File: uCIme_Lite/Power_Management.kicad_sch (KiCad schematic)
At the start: 17 parts

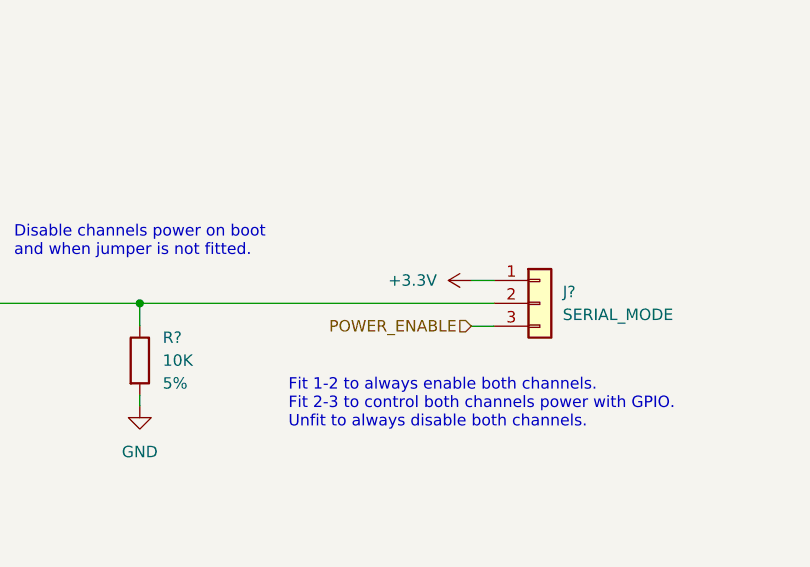
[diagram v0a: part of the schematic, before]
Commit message: lite: Used the +5V power supply for the power switch always-on mode instead of the +3.3V to ease routing.
Signed-off-by: Adrien Ricciardi <aricciardi@baylibre.com>
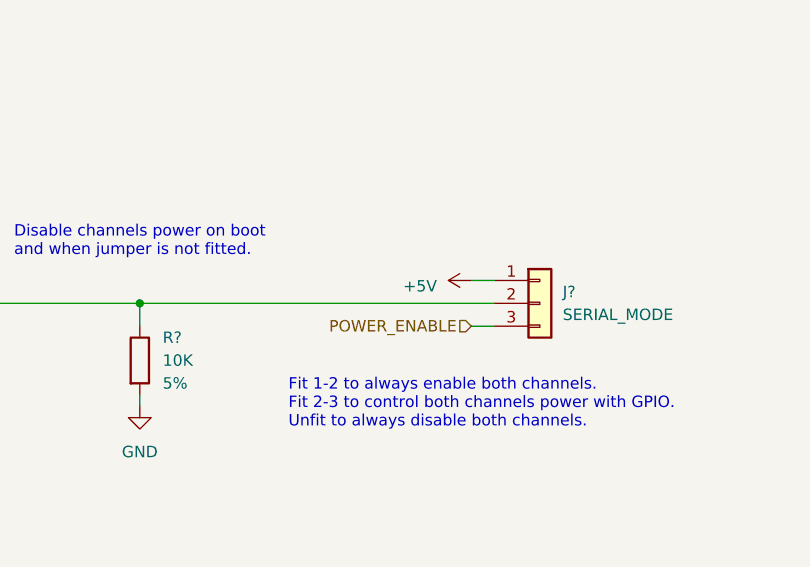
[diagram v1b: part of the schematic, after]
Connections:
- net +3.3V is gone; now on net +5V: J?.1 (Pin_1)
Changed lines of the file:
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@@
-    )
-  )
-  (symbol (lib_id "power:+3.3V") (at 250.19 58.42 90) (unit 1)
-    (in_bom yes) (on_board yes) (dnp no) (fields_autoplaced)
-    (property "Reference" "#PWR0117" (at 254 58.42 0)
-      (effects (font (size 1.27 1.27)) hide)
-    )
-    (property "Value" "+3.3V" (at 246.38 58.4199 90)
-      (effects (font (size 1.27 1.27)) (justify left))
-    )
-    (property "Footprint" "" (at 250.19 58.42 0)
-      (effects (font (size 1.27 1.27)) hide)
-    )
-    (property "Datasheet" "" (at 250.19 58.42 0)
-      (effects (font (size 1.27 1.27)) hide)
-    )
-    (pin "1")
-    (instances
-      (project "uCIme_Lite"
-        (path "/6d46d15a-8cd0-4983-b142-8248cafa0b56/b72074d7-db6e-4ce2-896d-216adccf1d19"
-          (reference "#PWR0117") (unit 1)
-        )
-      )
     )
   )
@@
         )
       )
+    )
+  )
+  (symbol (lib_id "power:+5V") (at 250.19 58.42 90) (unit 1)
+    (in_bom yes) (on_board yes) (dnp no) (fields_autoplaced)
+    (property "Reference" "#PWR01" (at 254 58.42 0)
+      (effects (font (size 1.27 1.27)) hide)
+    )
+    (property "Value" "+5V" (at 246.38 59.055 90)
+      (effects (font (size 1.27 1.27)) (justify left))
+    )
+    (property "Footprint" "" (at 250.19 58.42 0)
+      (effects (font (size 1.27 1.27)) hide)
+    )
+    (property "Datasheet" "" (at 250.19 58.42 0)
+      (effects (font (size 1.27 1.27)) hide)
+    )
+    (pin "1")
+    (instances
+      (project "uCIme_Lite"
+        (path "/6d46d15a-8cd0-4983-b142-8248cafa0b56/b72074d7-db6e-4ce2-896d-216adccf1d19"
+          (reference "#PWR01") (unit 1)
+        )
+      )

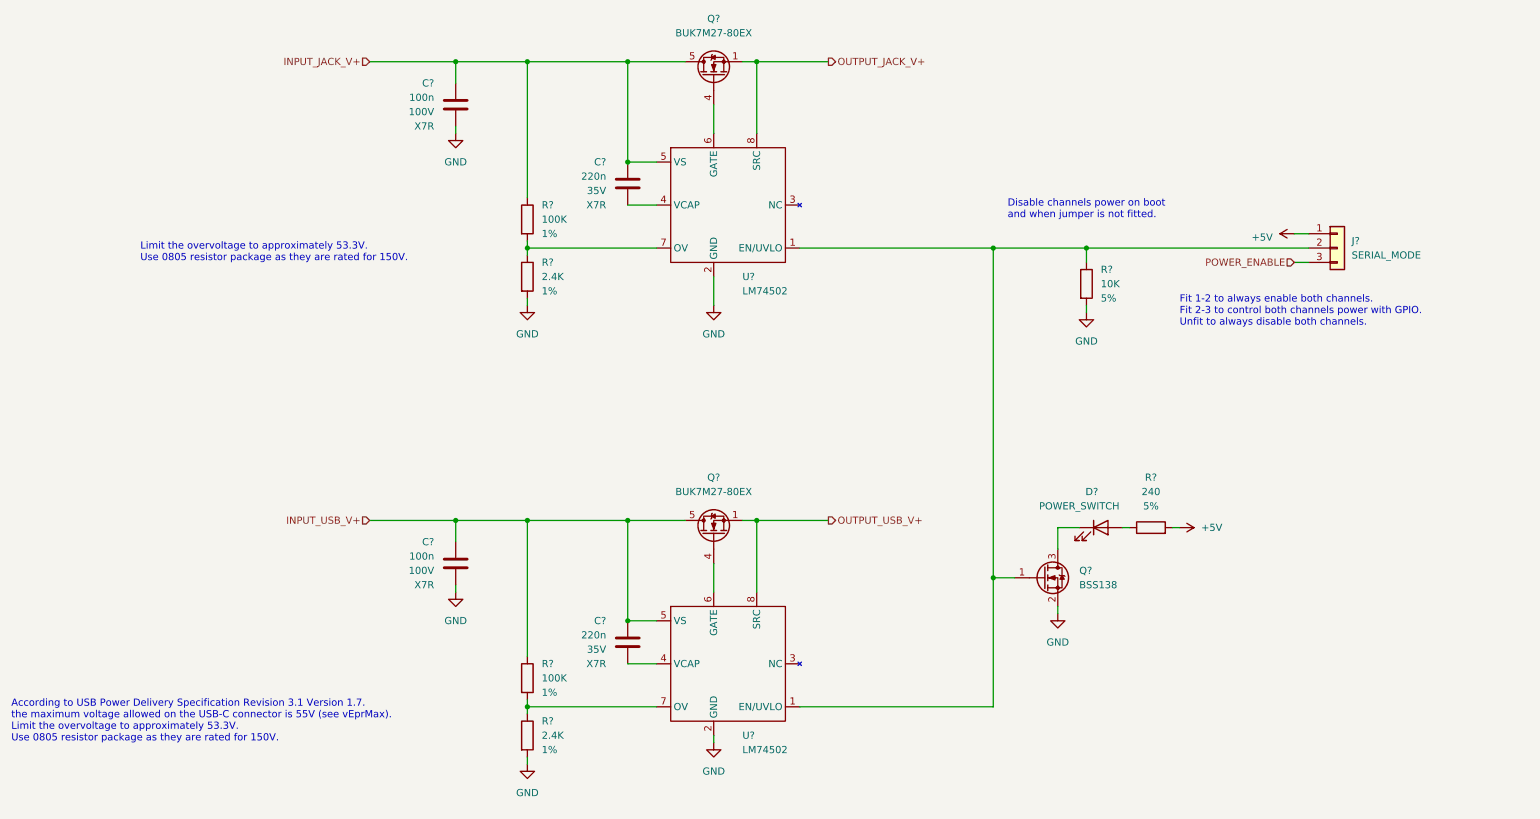
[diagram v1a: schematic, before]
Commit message: lite: Added a dedicated mode selection jumper per power channel. This allows to fit custom requirements, like disabling the USB power while keeping the USB connected and driving the board power with the jack channel.
Signed-off-by: Adrien Ricciardi <aricciardi@baylibre.com>
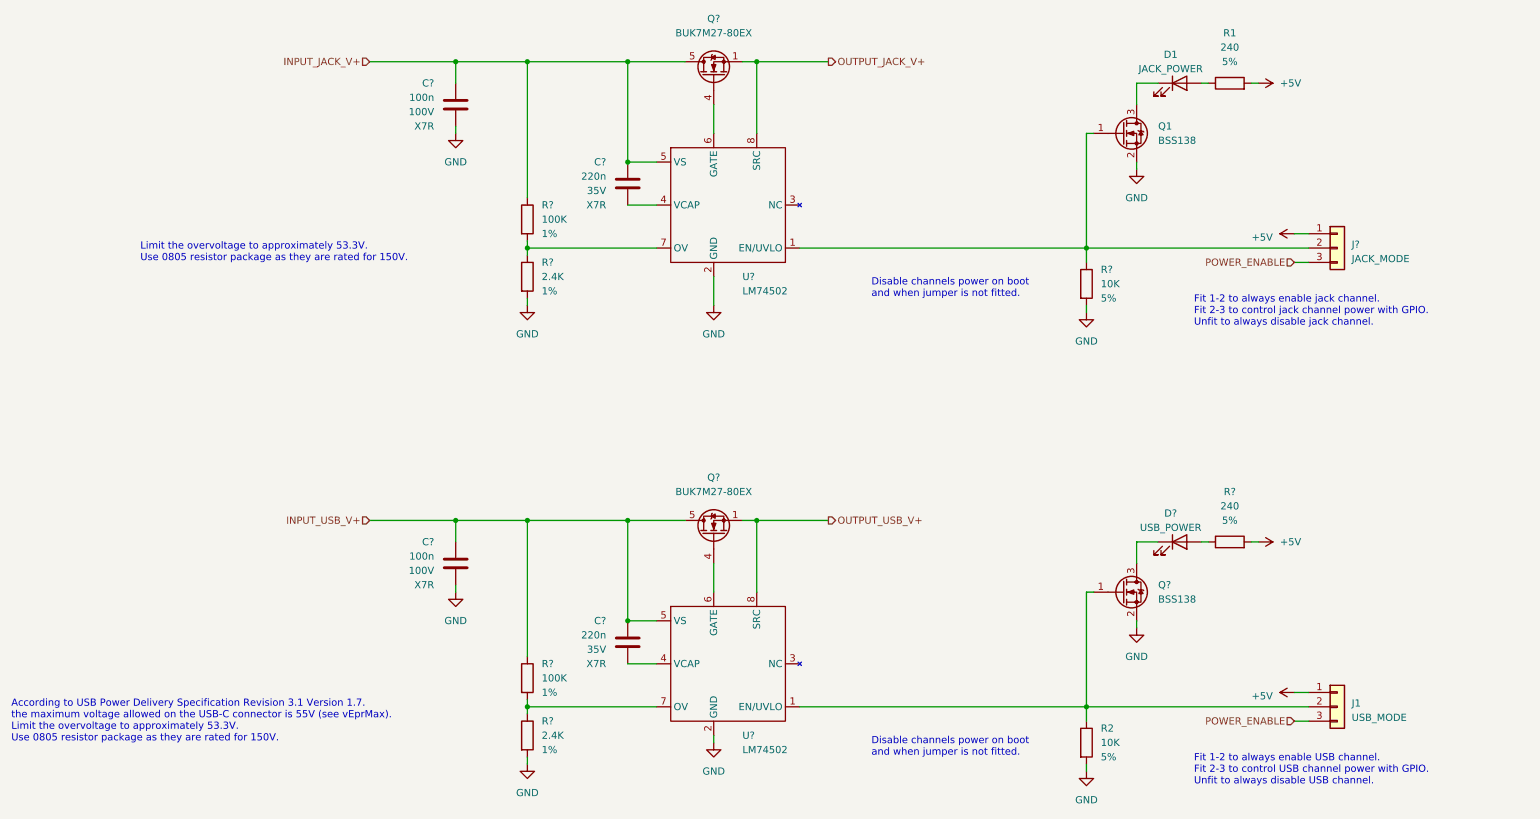
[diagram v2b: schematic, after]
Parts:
- added D1: POWER_SWITCH, symbol Device:LED
- added J1: USB_MODE, symbol Connector_Generic:Conn_01x03
- added Q1: BSS138, Package_TO_SOT_SMD:SOT-23, symbol Transistor_FET:BSS138
- added R1: 240, Resistor_SMD:R_1206_3216Metric, symbol Device:R
- added R2: 10K, Resistor_SMD:R_0603_1608Metric, symbol Device:R
- J?: value SERIAL_MODE -> JACK_MODE
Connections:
- net +5V: now also J1.1 (Pin_1), R1.2
- net GND: now also Q1.2 (S), R2.2
- net POWER_ENABLE: now also J1.3 (Pin_3)
- net at J?.2 (Pin_2), R?.1, U?.1 (EN/UVLO): now also Q1.1 (G); no longer Q?.1 (G), U?.1 (EN/UVLO)
- new net: D1.1 (K), Q1.3 (D)
- new net: D1.2 (A), R1.1
- new net: J1.2 (Pin_2), Q?.1 (G), R2.1, U?.1 (EN/UVLO)
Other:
- note added: "Fit 1-2 to always enable USB channel. Fit 2-3 to control USB channel power with GPIO. Unfit to always disable USB channel."
- note added: "Fit 1-2 to always enable jack channel. Fit 2-3 to control jack channel power with GPIO. Unfit to always disable jack channel."
- note removed: "Fit 1-2 to always enable both channels. Fit 2-3 to control both channels power with GPIO. Unfit to always disable both channels."
- moved on the sheet: D?, Q?, R?

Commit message: lite: Named components in the schematic and added some part numbers.
Signed-off-by: Adrien Ricciardi <aricciardi@baylibre.com>
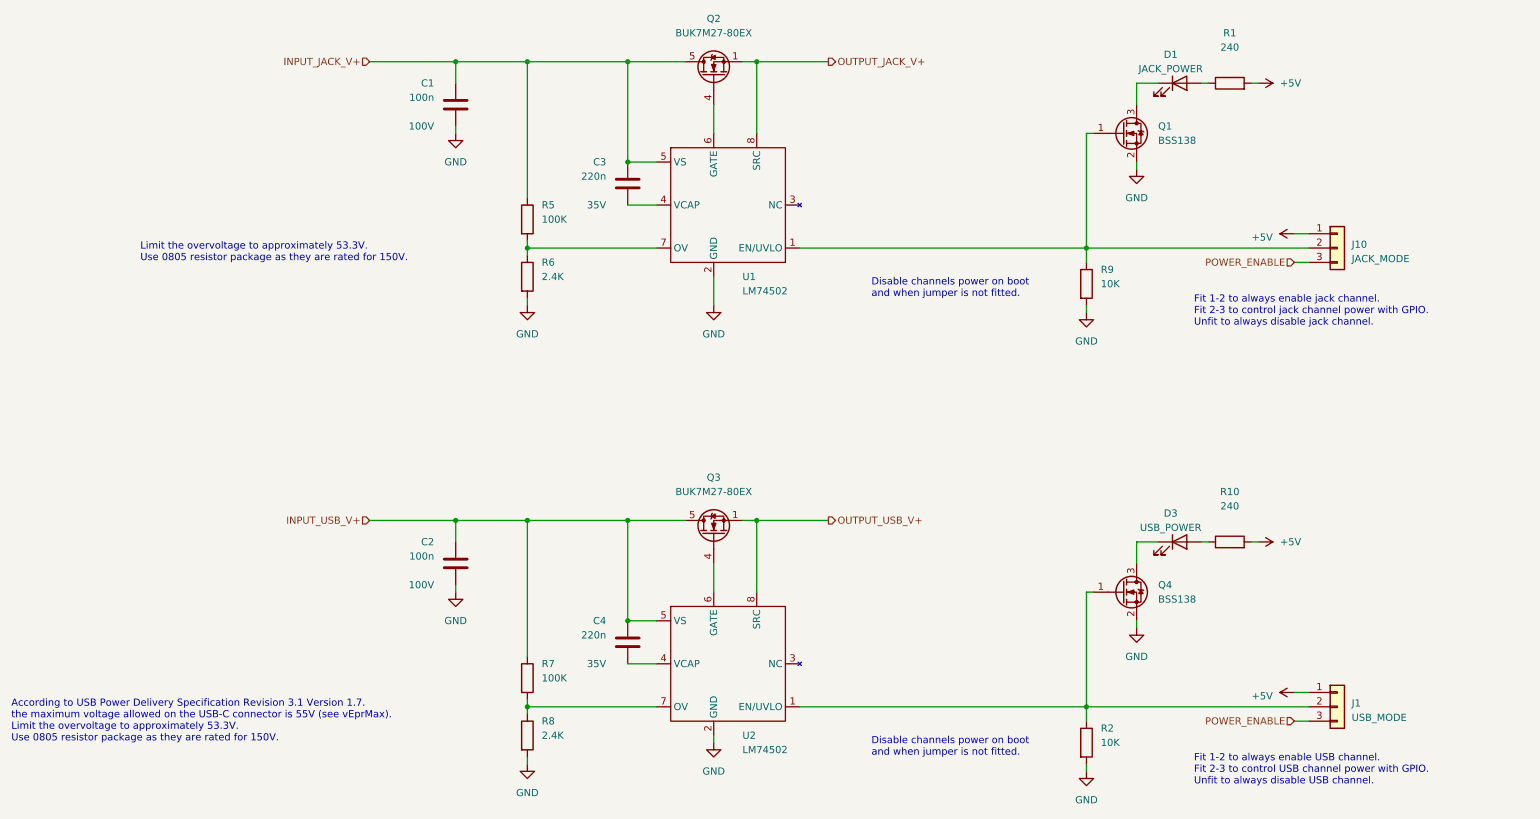
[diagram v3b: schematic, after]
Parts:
- C1, C2: renamed from C?; Value1 100V -> (none); Value2 X7R -> 100V; Value3 (none) -> X7R
- C3, C4: renamed from C?; Value1 35V -> (none); Value2 X7R -> 35V; Value3 (none) -> X7R
- R1, R2: Value1 5% -> (none); Value2 (none) -> 5%
- R10, R9: renamed from R?; Value1 5% -> (none); Value2 (none) -> 5%
- R5, R6, R7, R8: renamed from R?; Value1 1% -> (none); Value2 (none) -> 1%
- U1, U2: renamed from U?; PartNumber (none) -> LM74502DDFR
- gave numbers to parts that had none: 5
